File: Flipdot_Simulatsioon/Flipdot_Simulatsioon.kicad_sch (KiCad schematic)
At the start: 4 parts

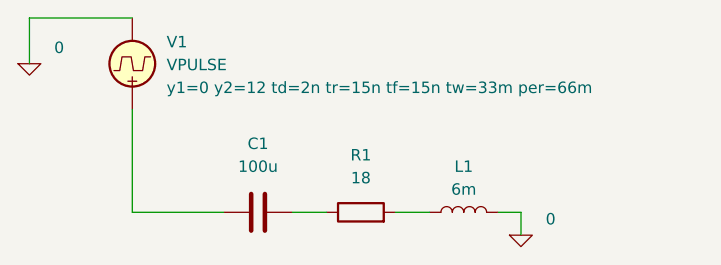
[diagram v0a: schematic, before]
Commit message: simulatsiooni check 50u kondekaid vaja
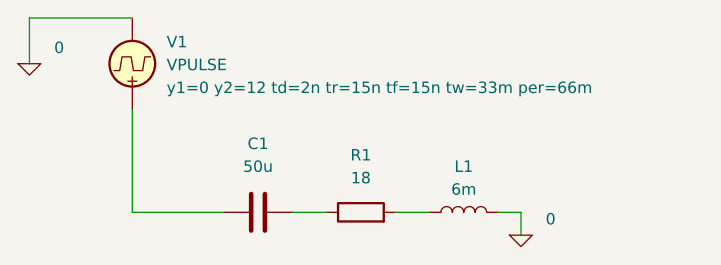
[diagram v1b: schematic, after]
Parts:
- C1: value 100u -> 50u
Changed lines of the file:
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@@
 			)
 		)
-		(property "Value" "100u"
+		(property "Value" "50u"
 			(at 96.52 176.53 90)
 			(effects

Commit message: Kaareli tagasiside
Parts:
- C1: value 50u -> 20u
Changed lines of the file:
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@@
 			)
 		)
-		(property "Value" "50u"
+		(property "Value" "20u"
 			(at 96.52 176.53 90)
 			(effects
@@
 			)
 		)
-		(property "Sim.Params" "y1=0 y2=12 td=2n tr=15n tf=15n tw=33m per=66m"
+		(property "Sim.Params" "y1=0 y2=24 td=2n tr=15n tf=15n tw=33m per=66m"
 			(at 86.36 167.7697 0)
 			(effects
